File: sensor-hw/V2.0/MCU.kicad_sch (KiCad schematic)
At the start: 35 parts, among them SW1 SW_MEC_5E, U2 STM32WL55JCI7, x2 NX2012SA 32.768KHz

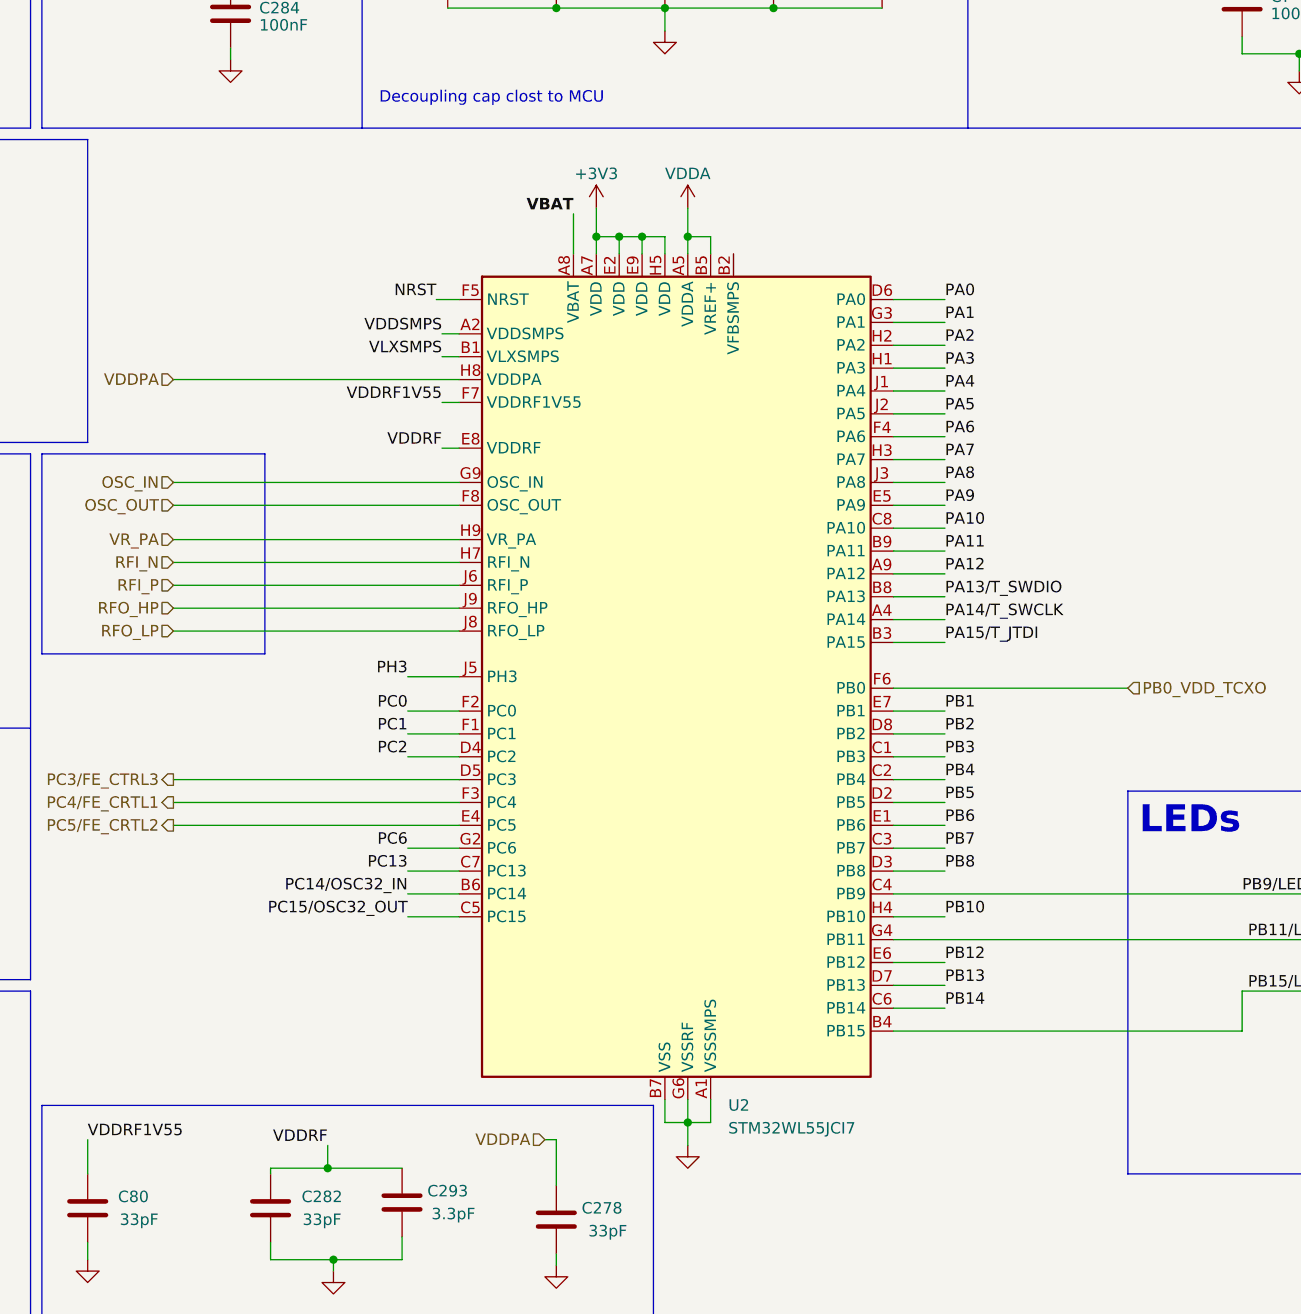
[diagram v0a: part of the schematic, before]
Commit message: rearranged heirchal block wiring for better representation.
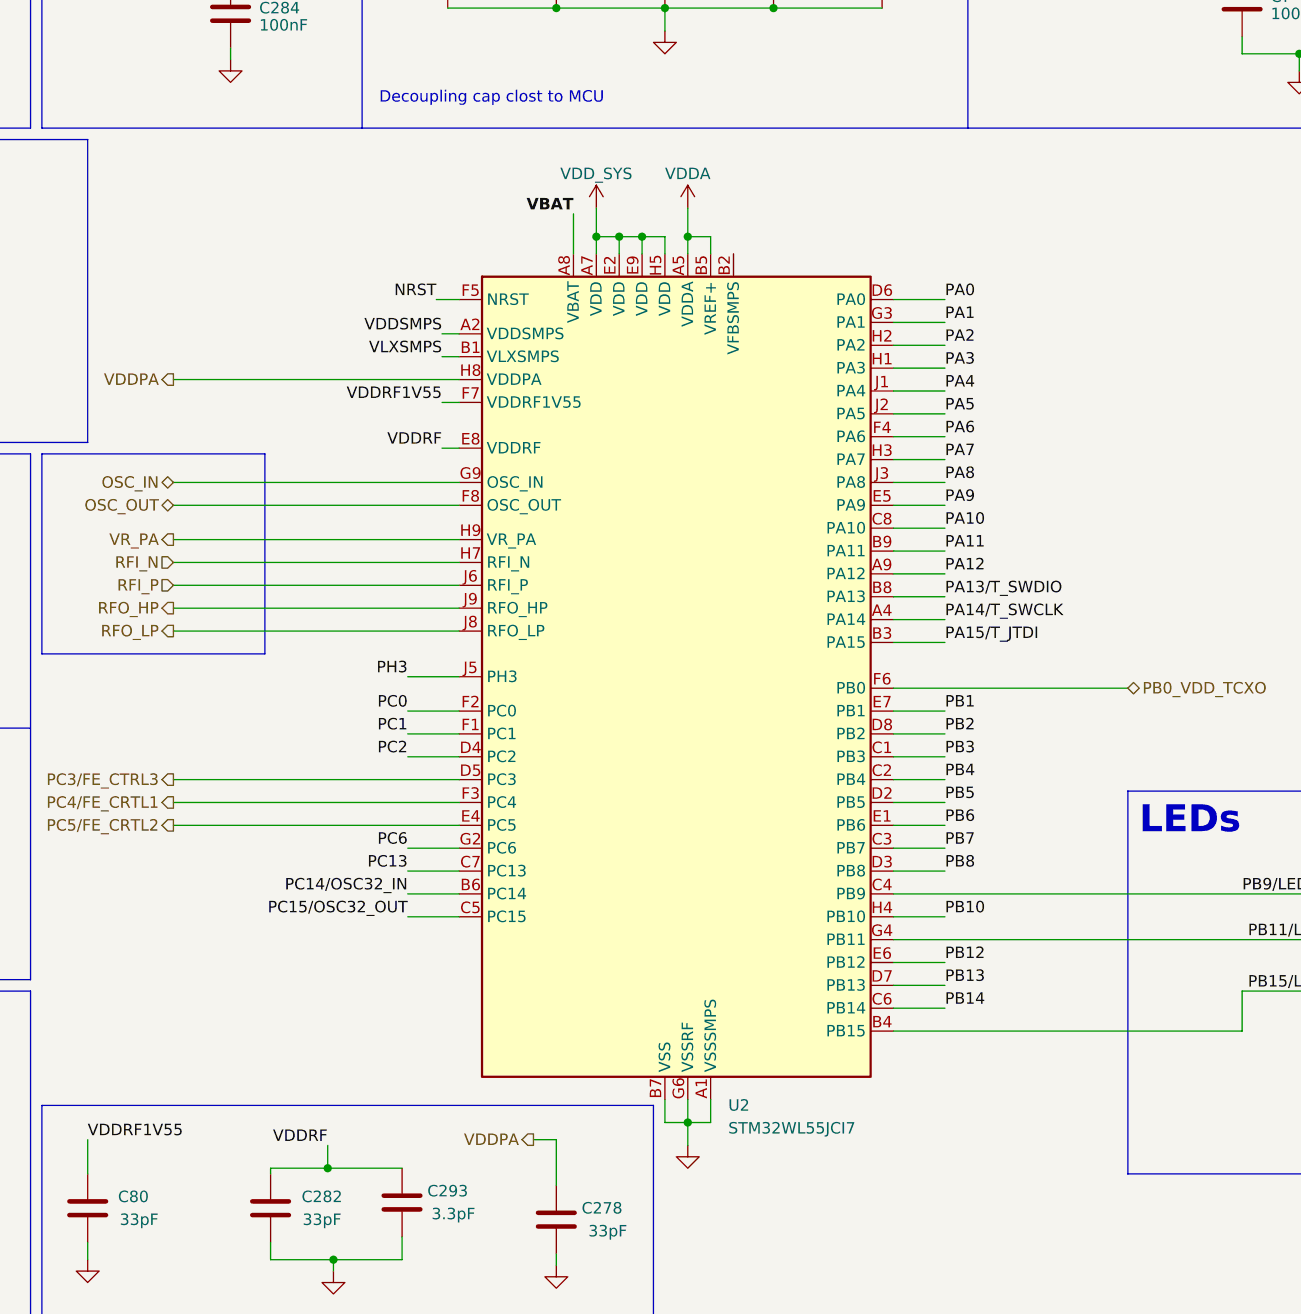
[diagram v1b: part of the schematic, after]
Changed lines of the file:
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@@
     (stroke (width 0) (type default))
   )
-  (wire (pts (xy 130.175 158.75) (xy 131.445 158.75))
+  (wire (pts (xy 128.905 158.75) (xy 131.445 158.75))
     (stroke (width 0) (type default))
   )
@@
     (effects (font (size 1.27 1.27)) (justify left bottom))
   )
-  (hierarchical_label "PB0_VDD_TCXO" (shape input) (at 194.945 108.585 0) (fields_autoplaced)
+  (hierarchical_label "PB0_VDD_TCXO" (shape bidirectional) (at 194.945 108.585 0) (fields_autoplaced)
     (effects (font (size 1.27 1.27)) (justify left))
   )
@@
     (effects (font (size 1.27 1.27)) (justify right))
   )
-  (hierarchical_label "VDDPA" (shape input) (at 88.9 74.295 180) (fields_autoplaced)
+  (hierarchical_label "VDDPA" (shape output) (at 128.905 158.75 180) (fields_autoplaced)
+    (effects (font (size 1.27 1.27)) (justify right))
+  )
+  (hierarchical_label "VDDPA" (shape output) (at 88.9 74.295 180) (fields_autoplaced)
     (effects (font (size 1.27 1.27)) (justify right))
   )
@@
     (effects (font (size 1.27 1.27)) (justify left))
   )
-  (hierarchical_label "RFO_HP" (shape input) (at 88.9 99.695 180) (fields_autoplaced)
+  (hierarchical_label "RFO_HP" (shape output) (at 88.9 99.695 180) (fields_autoplaced)
     (effects (font (size 1.27 1.27)) (justify right))
   )
@@
     (effects (font (size 1.27 1.27)) (justify right))
   )
-  (hierarchical_label "VDDPA" (shape input) (at 130.175 158.75 180) (fields_autoplaced)
-    (effects (font (size 1.27 1.27)) (justify right))
-  )
-  (hierarchical_label "RFO_LP" (shape input) (at 88.9 102.235 180) (fields_autoplaced)
+  (hierarchical_label "RFO_LP" (shape output) (at 88.9 102.235 180) (fields_autoplaced)
     (effects (font (size 1.27 1.27)) (justify right))
   )
@@
     (effects (font (size 1.27 1.27)) (justify right))
   )
-  (hierarchical_label "OSC_OUT" (shape input) (at 88.9 88.265 180) (fields_autoplaced)
+  (hierarchical_label "OSC_OUT" (shape bidirectional) (at 88.9 88.265 180) (fields_autoplaced)
     (effects (font (size 1.27 1.27)) (justify right))
   )
@@
     (effects (font (size 1.27 1.27)) (justify right))
   )
-  (hierarchical_label "OSC_IN" (shape input) (at 88.9 85.725 180) (fields_autoplaced)
+  (hierarchical_label "OSC_IN" (shape bidirectional) (at 88.9 85.725 180) (fields_autoplaced)
     (effects (font (size 1.27 1.27)) (justify right))
   )
@@
     (effects (font (size 1.27 1.27)) (justify left))
   )
-  (hierarchical_label "VR_PA" (shape input) (at 88.9 92.075 180) (fields_autoplaced)
+  (hierarchical_label "VR_PA" (shape output) (at 88.9 92.075 180) (fields_autoplaced)
     (effects (font (size 1.27 1.27)) (justify right))
   )
@@
         (path "/55528413-c8da-463c-8fa0-4d866d881d6a/518ff5f7-f453-4b34-9ad0-58dfc1ce712d"
           (reference "D2") (unit 1)
-        )
-      )
-    )
-  )
-  (symbol (lib_id "power:+3V3") (at 135.89 55.245 0) (unit 1)
-    (in_bom yes) (on_board yes) (dnp no) (fields_autoplaced)
-    (property "Reference" "#PWR021" (at 135.89 59.055 0)
-      (effects (font (size 1.27 1.27)) hide)
-    )
-    (property "Value" "+3V3" (at 135.89 51.435 0)
-      (effects (font (size 1.27 1.27)))
-    )
-    (property "Footprint" "" (at 135.89 55.245 0)
-      (effects (font (size 1.27 1.27)) hide)
-    )
-    (property "Datasheet" "" (at 135.89 55.245 0)
-      (effects (font (size 1.27 1.27)) hide)
-    )
-    (pin "1")
-    (instances
-      (project "beta_prototype"
-        (path "/39c3f2e4-c15d-4dcf-8488-7b897a1552e9/658c19c7-b807-4513-9e9a-59370c911264"
-          (reference "#PWR021") (unit 1)
-        )
-      )
-      (project "sensor-hw"
-        (path "/55528413-c8da-463c-8fa0-4d866d881d6a/518ff5f7-f453-4b34-9ad0-58dfc1ce712d"
-          (reference "#PWR021") (unit 1)
         )
       )
@@
         )
       )
+    )
+  )
+  (symbol (lib_name "+3V3_1") (lib_id "power:+3V3") (at 135.89 55.245 0) (unit 1)
+    (in_bom yes) (on_board yes) (dnp no)
+    (property "Reference" "#PWR020" (at 135.89 59.055 0)
+      (effects (font (size 1.27 1.27)) hide)
+    )
+    (property "Value" "VDD_SYS" (at 135.89 51.435 0)
+      (effects (font (size 1.27 1.27)))
+    )
+    (property "Footprint" "" (at 135.89 55.245 0)
+      (effects (font (size 1.27 1.27)) hide)
+    )
+    (property "Datasheet" "" (at 135.89 55.245 0)
+      (effects (font (size 1.27 1.27)) hide)
+    )
+    (property "value2" "" (at 135.89 55.245 0)
+      (effects (font (size 1.27 1.27)))
+    )
+    (property "Supplier- Part Number" "" (at 135.89 55.245 0)
+      (effects (font (size 1.27 1.27)) hide)
+    )
+    (property "Manufacturer Product Number" "" (at 135.89 55.245 0)
+      (effects (font (size 1.27 1.27)) hide)
+    )
+    (property "supplier Link" "" (at 135.89 55.245 0)
+      (effects (font (size 1.27 1.27)) hide)
+    )
+    (property "Manufacturer" "" (at 135.89 55.245 0)
+      (effects (font (size 1.27 1.27)) hide)
+    )
+    (pin "1")
+    (instances
+      (project "beta_prototype"
+        (path "/39c3f2e4-c15d-4dcf-8488-7b897a1552e9/658c19c7-b807-4513-9e9a-59370c911264"
+          (reference "#PWR020") (unit 1)
+        )
+      )
+      (project "sensor-hw"
+        (path "/55528413-c8da-463c-8fa0-4d866d881d6a/518ff5f7-f453-4b34-9ad0-58dfc1ce712d"
+          (reference "#PWR02") (unit 1)
+        )
+      )

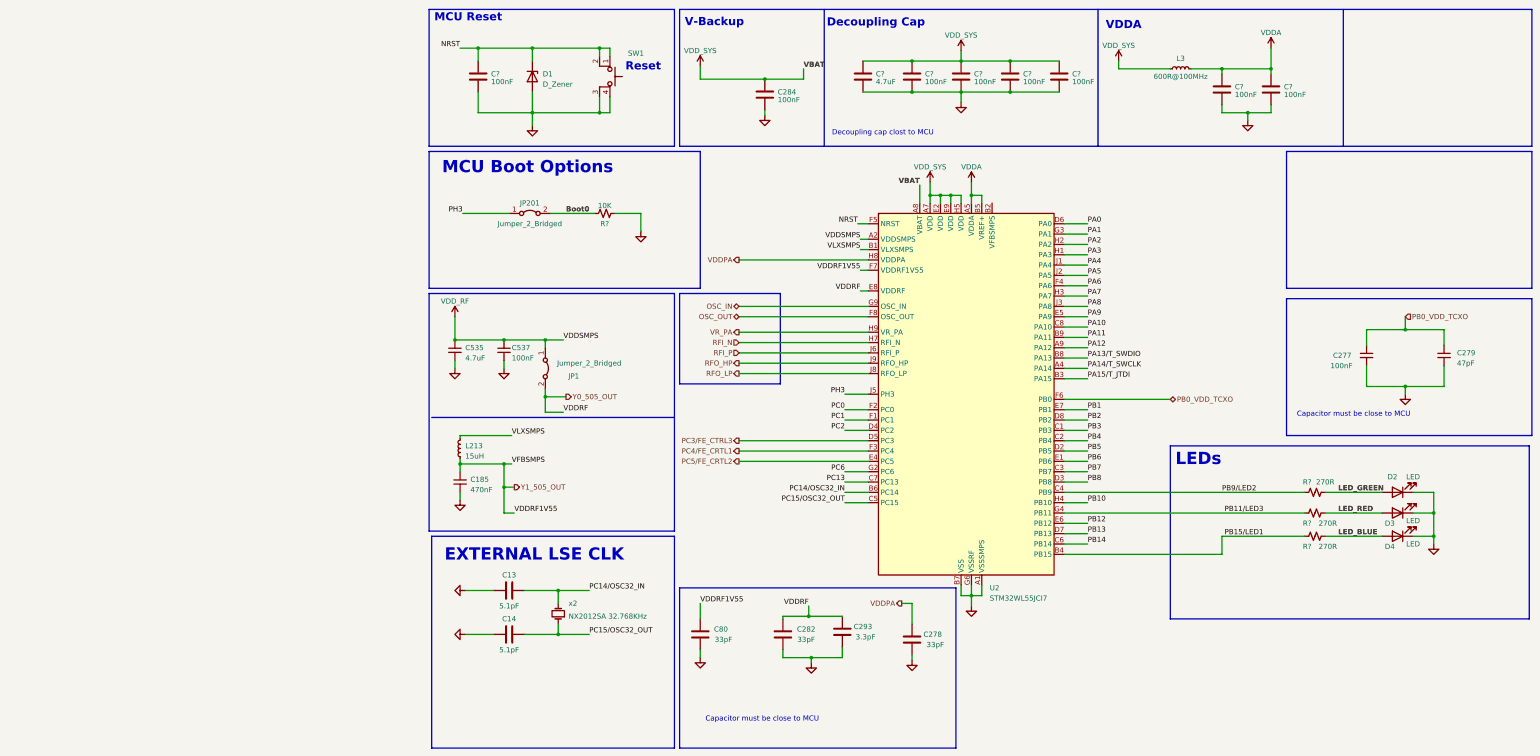
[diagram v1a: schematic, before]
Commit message: Added the Power section.
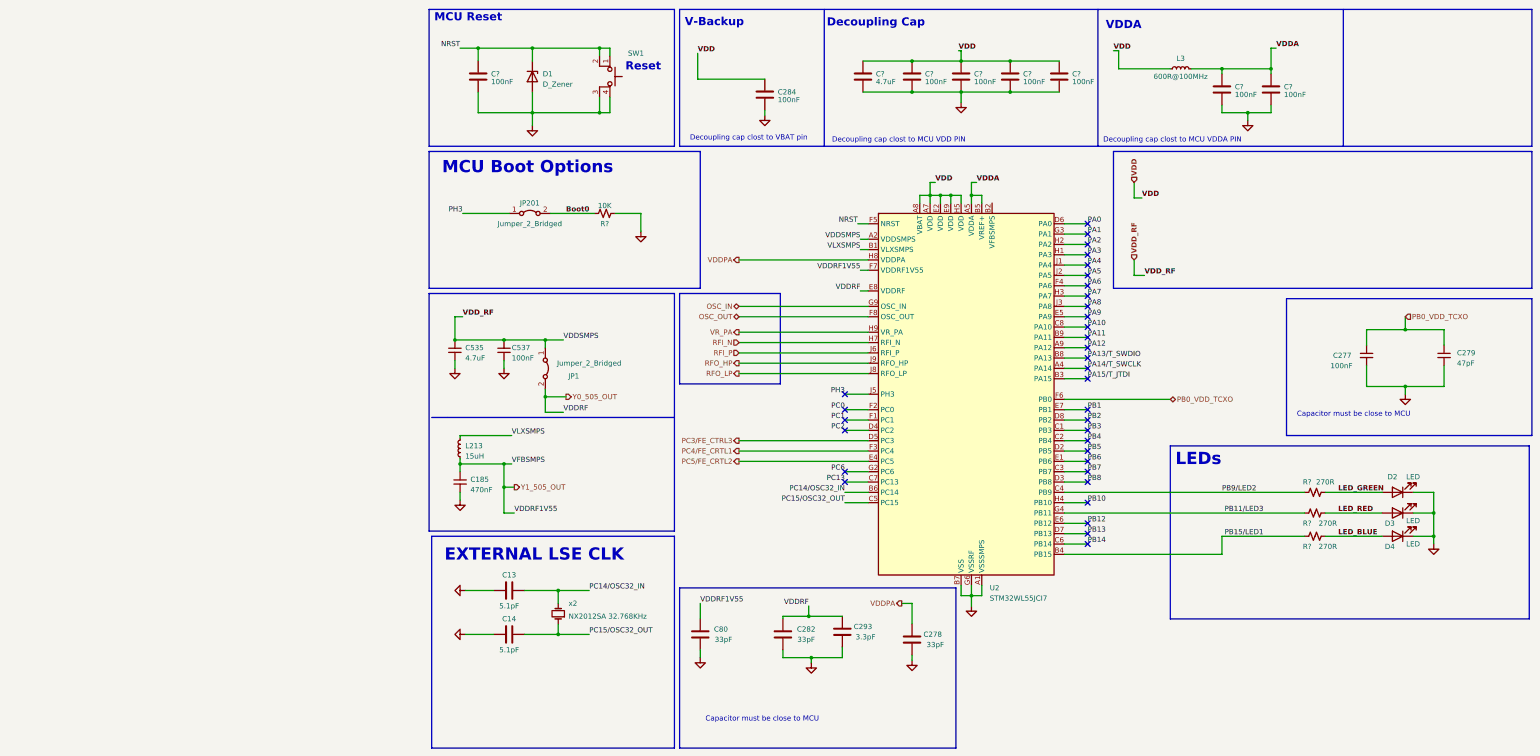
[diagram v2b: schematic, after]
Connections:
- net +3V3 renamed VDD
- net VDD: no longer C535.1, C537.1, JP1.1 (A), U2.A2 (VDDSMPS)
- new net VDD_RF: C535.1, C537.1, JP1.1 (A), U2.A2 (VDDSMPS)
- no-connect marks 0 -> 34
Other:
- note added: "Decoupling cap clost to MCU VDD PIN"
- note added: "Decoupling cap clost to MCU VDDA PIN"
- note added: "Decoupling cap clost to VBAT pin"
- note removed: "Decoupling cap clost to MCU"
